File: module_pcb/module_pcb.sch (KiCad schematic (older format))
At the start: 106 parts, among them J1 ISP, J2 US, J3 DS, Q1 HSS2307, Q2 BSS123, U1 W25Q16JV, U2 AP1117-33, U3 TPS563200, U5 ATmega328P-AU, U7 74LVC1G34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

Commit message: Renamed a few things
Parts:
- U1: symbol Module_PCB:W25Q16JV -> module_pcb:W25Q16JV
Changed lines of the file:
@@
 $EndComp
 $Comp
-L Module_PCB:W25Q16JV U1
+L module_pcb:W25Q16JV U1
 U 1 1 60D73EDF
 P 1100 6550

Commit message: Updated output files for module_pcb
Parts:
- BT1, H1, H2, H3, H4, H5, H7, TP1, TP2: MPN (none) -> DNP; Manufacturer (none) -> DNP
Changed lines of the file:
@@
 F 2 "MountingHole:MountingHole_3.2mm_M3_Pad" H 6250 5250 50  0001 C CNN
 F 3 "~" H 6250 5250 50  0001 C CNN
+F 4 "DNP" H 6250 5250 50  0001 C CNN "MPN"
+F 5 "DNP" H 6250 5250 50  0001 C CNN "Manufacturer"
 	1    6250 5250
 	1    0    0    -1
@@
 F 2 "MountingHole:MountingHole_3.2mm_M3_Pad" H 6250 5550 50  0001 C CNN
 F 3 "~" H 6250 5550 50  0001 C CNN
+F 4 "DNP" H 6250 5550 50  0001 C CNN "MPN"
+F 5 "DNP" H 6250 5550 50  0001 C CNN "Manufacturer"
 	1    6250 5550
 	1    0    0    -1
@@
 F 2 "MountingHole:MountingHole_3.2mm_M3_Pad" H 6250 5850 50  0001 C CNN
 F 3 "~" H 6250 5850 50  0001 C CNN
+F 4 "DNP" H 6250 5850 50  0001 C CNN "MPN"
+F 5 "DNP" H 6250 5850 50  0001 C CNN "Manufacturer"
 	1    6250 5850
 	1    0    0    -1
@@
 F 2 "MountingHole:MountingHole_3.2mm_M3_Pad" H 7150 5250 50  0001 C CNN
 F 3 "~" H 7150 5250 50  0001 C CNN
+F 4 "DNP" H 7150 5250 50  0001 C CNN "MPN"
+F 5 "DNP" H 7150 5250 50  0001 C CNN "Manufacturer"
 	1    7150 5250
 	1    0    0    -1
@@
 F 2 "MountingHole:MountingHole_3.2mm_M3_Pad" H 7150 5550 50  0001 C CNN
 F 3 "~" H 7150 5550 50  0001 C CNN
+F 4 "DNP" H 7150 5550 50  0001 C CNN "MPN"
+F 5 "DNP" H 7150 5550 50  0001 C CNN "Manufacturer"
 	1    7150 5550
 	1    0    0    -1
@@
 F 2 "MountingHole:MountingHole_3.2mm_M3_Pad" H 7150 5850 50  0001 C CNN
 F 3 "~" H 7150 5850 50  0001 C CNN
+F 4 "DNP" H 7150 5850 50  0001 C CNN "MPN"
+F 5 "DNP" H 7150 5850 50  0001 C CNN "Manufacturer"
 	1    7150 5850
 	1    0    0    -1
@@
 F 2 "TestPoint:TestPoint_Pad_D1.5mm" H 1300 5800 50  0001 C CNN
 F 3 "~" H 1300 5800 50  0001 C CNN
+F 4 "DNP" H 1100 5800 50  0001 C CNN "MPN"
+F 5 "DNP" H 1100 5800 50  0001 C CNN "Manufacturer"
 	1    1100 5800
 	1    0    0    -1
@@
 F 2 "TestPoint:TestPoint_Pad_D1.5mm" H 1600 5800 50  0001 C CNN
 F 3 "~" H 1600 5800 50  0001 C CNN
+F 4 "DNP" H 1400 5800 50  0001 C CNN "MPN"
+F 5 "DNP" H 1400 5800 50  0001 C CNN "Manufacturer"
 	1    1400 5800
 	1    0    0    -1
@@
 F 2 "Connector_PinHeader_2.54mm:PinHeader_2x01_P2.54mm_Vertical" V 950 1510 50  0001 C CNN
 F 3 "~" V 950 1510 50  0001 C CNN
+F 4 "DNP" H 950 1450 50  0001 C CNN "MPN"
+F 5 "DNP" H 950 1450 50  0001 C CNN "Manufacturer"
 	1    950  1450
 	1    0    0    -1

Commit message: Updated gerber files
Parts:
- Q2: Manufacturer ON Semiconductor -> Changjiang Electronics Tech (CJ)
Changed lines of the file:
@@
 F 2 "Package_TO_SOT_SMD:SOT-23" H 2850 1575 50  0001 L CIN
 F 3 "http://www.diodes.com/assets/Datasheets/ds30366.pdf" H 2650 1650 50  0001 L CNN
-F 4 "ON Semiconductor" H 2650 1650 50  0001 C CNN "Manufacturer"
+F 4 "Changjiang Electronics Tech (CJ) " H 2650 1650 50  0001 C CNN "Manufacturer"
 F 5 "BSS123" H 2650 1650 50  0001 C CNN "MPN"
 	1    2650 1650

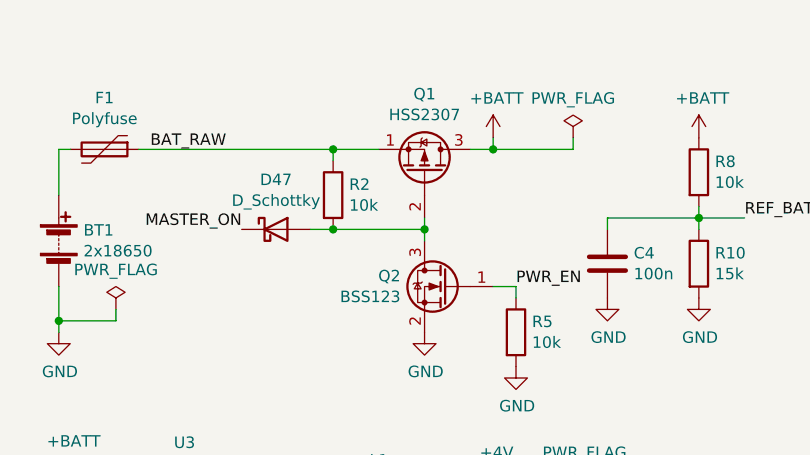
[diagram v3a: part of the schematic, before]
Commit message: Fixed wrong pinout of p-channel mosfet for power control on main pcb and module pcb
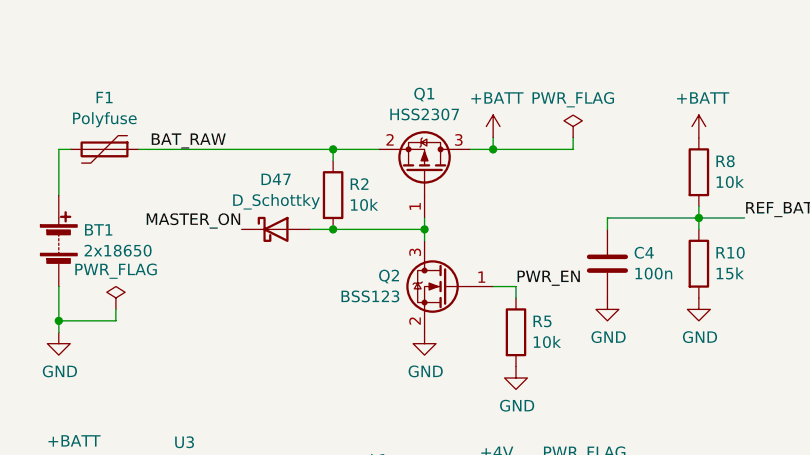
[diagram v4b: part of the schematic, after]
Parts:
- removed Q1: HSS2307, Package_TO_SOT_SMD:SOT-23W, symbol Device:Q_PMOS_SGD
- added Q1: HSS2307, Package_TO_SOT_SMD:SOT-23W, symbol Device:Q_PMOS_GSD
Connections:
- net +BATT: now also Q1.3 (D)
- net BAT_RAW: now also Q1.2 (S)
- net at D47.2 (A), Q2.3 (D), R2.2: now also Q1.1 (G)
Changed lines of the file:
@@
 Wire Wire Line
 	3350 1350 3350 1400
-$Comp
-L Device:Q_PMOS_SGD Q1
-U 1 1 60F2C1CF
-P 2550 1150
-F 0 "Q1" V 2892 1150 50  0000 C CNN
-F 1 "HSS2307" V 2801 1150 50  0000 C CNN
-F 2 "Package_TO_SOT_SMD:SOT-23W" H 2750 1250 50  0001 C CNN
-F 3 "~" H 2550 1150 50  0001 C CNN
-F 4 "HSS2307" H 2550 1150 50  0001 C CNN "MPN"
-F 5 "Huashuo" H 2550 1150 50  0001 C CNN "Manufacturer"
-	1    2550 1150
-	0    1    -1   0
-$EndComp
 Text Label 3200 6000 0    50   ~ 0
 PWR_EN
@@
 	3250 2550 3250 2600
 Connection ~ 3250 2600
+$Comp
+L Device:Q_PMOS_GSD Q1
+U 1 1 6192F199
+P 2550 1150
+F 0 "Q1" V 2892 1150 50  0000 C CNN
+F 1 "HSS2307" V 2801 1150 50  0000 C CNN
+F 2 "Package_TO_SOT_SMD:SOT-23W" H 2750 1250 50  0001 C CNN
+F 3 "~" H 2550 1150 50  0001 C CNN
+F 4 "HSS2307" H 2550 1150 50  0001 C CNN "MPN"
+F 5 "Huashuo" H 2550 1150 50  0001 C CNN "Manufacturer"
+	1    2550 1150
+	0    1    -1   0
+$EndComp
 $EndSCHEMATC

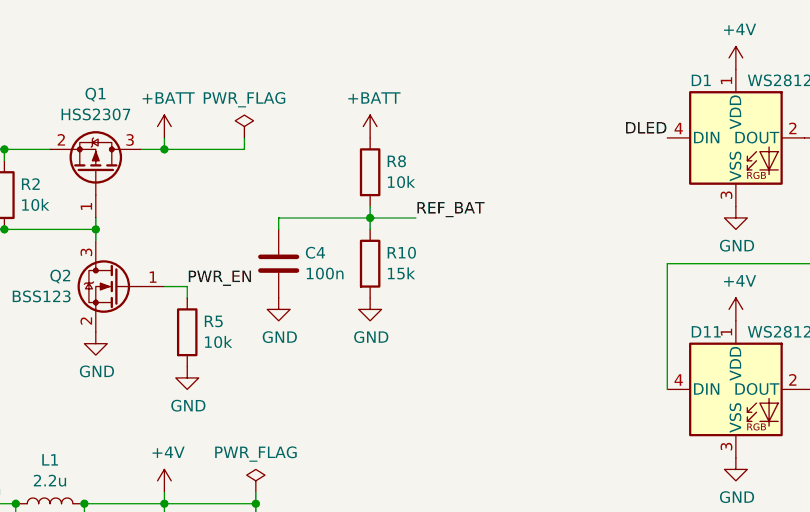
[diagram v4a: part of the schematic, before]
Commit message: Changed voltage divider fot battery measurement
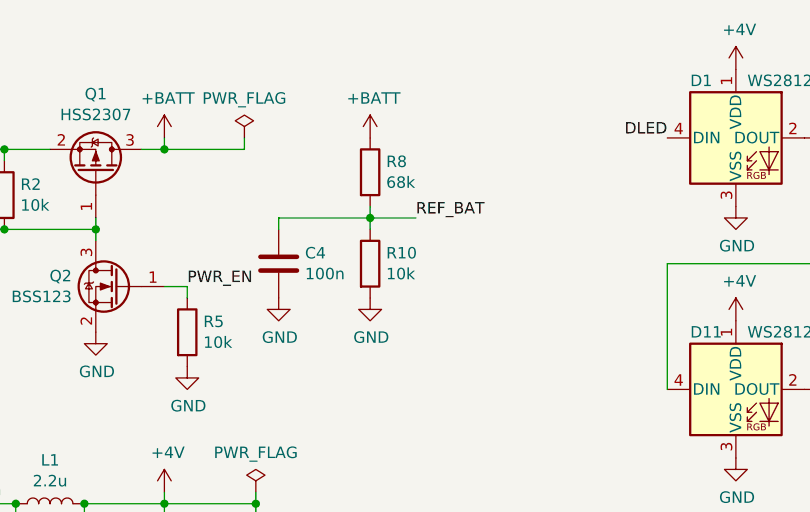
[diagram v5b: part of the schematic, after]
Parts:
- R10: value 15k -> 10k; MPN RC0603FR-0715KL -> RC0603JR-0710KL
- R8: value 10k -> 68k; MPN RC0603FR-0710KL -> RC0603JR-0768KL
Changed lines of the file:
@@
 P 3750 1550
 F 0 "R10" H 3820 1596 50  0000 L CNN
-F 1 "15k" H 3820 1505 50  0000 L CNN
+F 1 "10k" H 3820 1505 50  0000 L CNN
 F 2 "Resistor_SMD:R_0603_1608Metric" V 3680 1550 50  0001 C CNN
 F 3 "~" H 3750 1550 50  0001 C CNN
 F 4 "YAGEO" H 3750 1550 50  0001 C CNN "Manufacturer"
-F 5 "RC0603FR-0715KL" H 3750 1550 50  0001 C CNN "MPN"
+F 5 "RC0603JR-0710KL" H 3750 1550 50  0001 C CNN "MPN"
 	1    3750 1550
 	1    0    0    -1
@@
 P 3750 1150
 F 0 "R8" H 3820 1196 50  0000 L CNN
-F 1 "10k" H 3820 1105 50  0000 L CNN
+F 1 "68k" H 3820 1105 50  0000 L CNN
 F 2 "Resistor_SMD:R_0603_1608Metric" V 3680 1150 50  0001 C CNN
 F 3 "~" H 3750 1150 50  0001 C CNN
 F 4 "YAGEO" H 3750 1150 50  0001 C CNN "Manufacturer"
-F 5 "RC0603FR-0710KL" H 3750 1150 50  0001 C CNN "MPN"
+F 5 "RC0603JR-0768KL" H 3750 1150 50  0001 C CNN "MPN"
 	1    3750 1150
 	1    0    0    -1
